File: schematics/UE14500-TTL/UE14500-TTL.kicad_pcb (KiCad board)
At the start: 2 copper layers, 76.8 x 99.1 mm, 43 parts, among them J1 Edge 1, J2 Edge 2, J3 5VDC IN, SW1 Power On, U1 74LS08, U10 74LS74, U11 74LS00, U12 74LS86, U13 74LS00, U14 74LS251, U15 74LS02, U16 74LS74, U2 74LS08, U3 74LS00, U4 74LS374, U5 74LS138, U6 74LS138, U7 74LS74, U8 74LS02, U9 74LS02

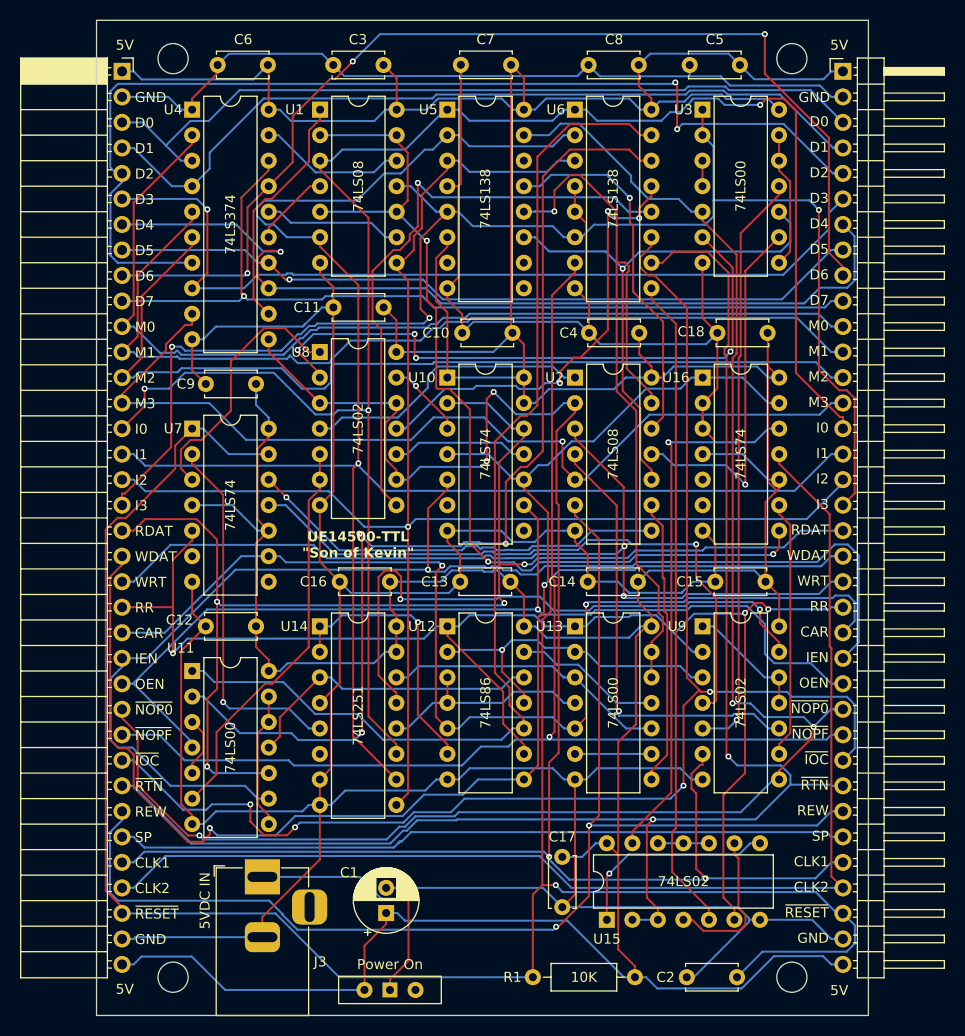
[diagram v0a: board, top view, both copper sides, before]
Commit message: Fix WRITE gating on processor board
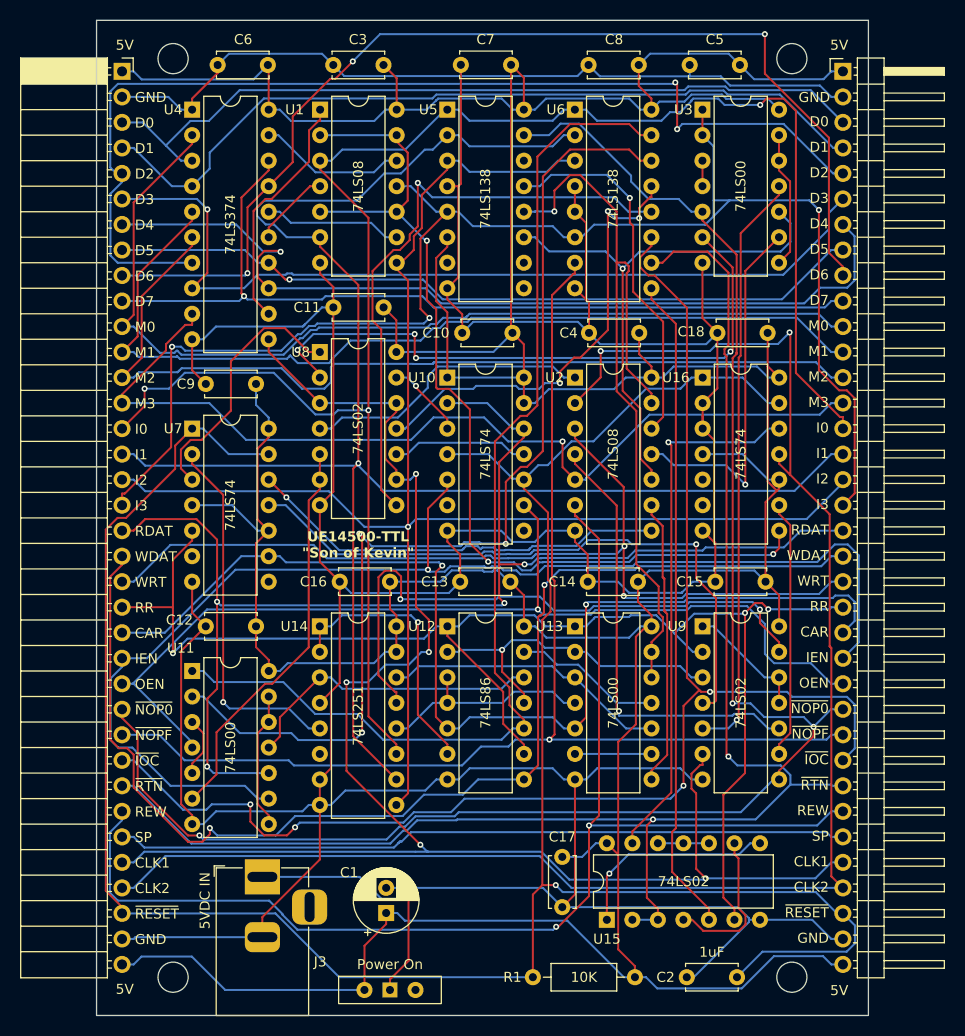
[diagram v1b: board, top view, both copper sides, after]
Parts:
- C2: value 100nF -> 1uF
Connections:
- U2 pad 2: CLK1 -> CLK2
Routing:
- net CLK2: track 120.4 -> 160.4 mm, vias 0 -> 2
- net CLK1: track 185.2 -> 162.4 mm, vias 4 -> 5
- net INST3: track 145.5 -> 147.7 mm

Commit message: Update the CPU schematic with V2 modifications
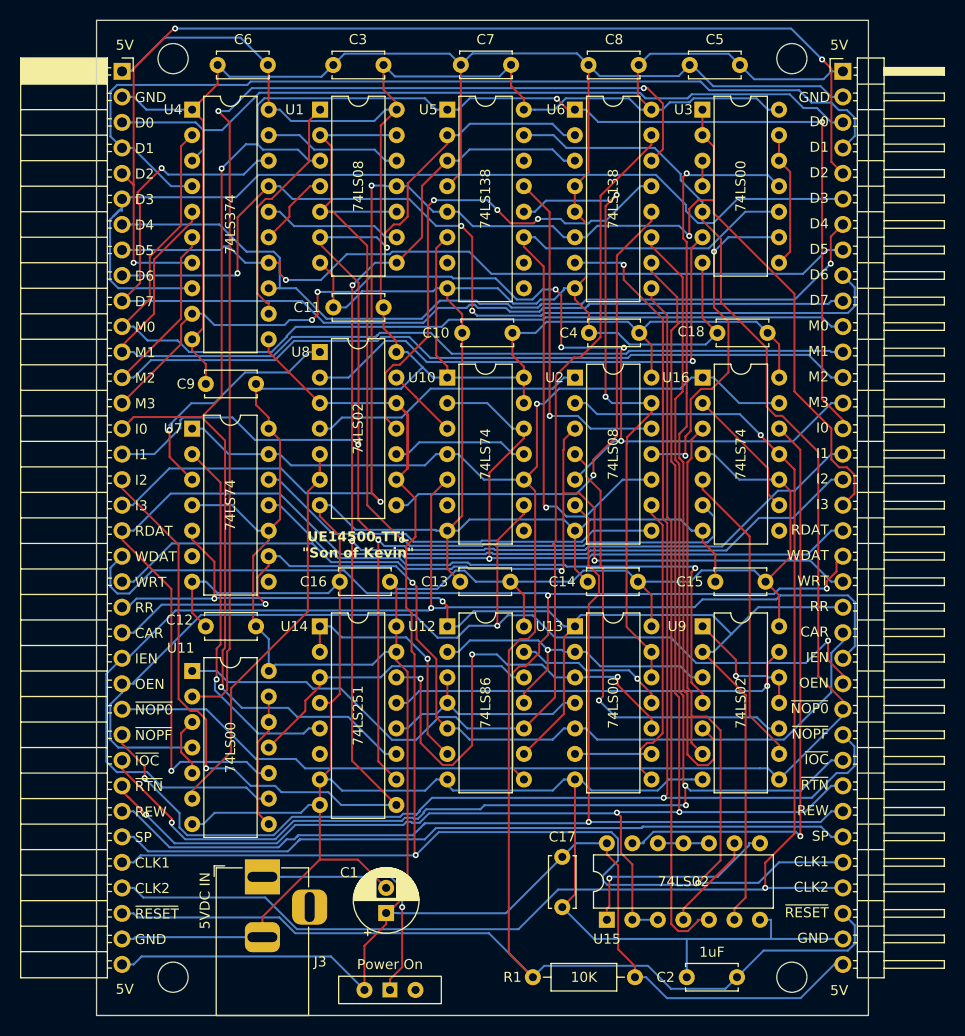
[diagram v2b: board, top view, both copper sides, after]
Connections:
- U16 pad 2: GND -> Net-(U16A-D)
- U16 pad 3: GND -> CLK1
- U16 pad 5: unconnected-(U16A-Q-Pad5) -> SKIP
- U16 pad 6: unconnected-(U16A-~{Q}-Pad6) -> ~{SKIP}
- U16 pad 8: ~{SKIP} -> unconnected-(U16B-~{Q}-Pad8)
- U16 pad 9: SKIP -> Net-(U16A-D)
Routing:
- net CLK1: track 162.4 -> 204.5 mm, vias 5 -> 2
- net ~{RESET}: track 244.4 -> 205.2 mm
- net INST2: track 156.9 -> 190.4 mm, vias 1 -> 3
- net ~{OP_NOPF}: track 123.1 -> 145.6 mm, vias 1 -> 3
- net WR_DATA: track 121.0 -> 101.9 mm
- net OR_RESULT: track 60.5 -> 41.5 mm, vias 2 -> 1
- net GND: track 499.7 -> 481.0 mm
- net NAND_RESULT: track 28.4 -> 46.8 mm, vias 0 -> 3
- net CLK2: track 160.4 -> 142.6 mm
- net REWIND: track 125.5 -> 108.0 mm, vias 2 -> 1
- net ~{LOAD_CAR}: track 58.6 -> 75.4 mm
- net D7: track 87.7 -> 101.3 mm
- net ~{OP_SUB}: track 78.3 -> 64.7 mm, vias 1 -> 2
- net D1: track 80.6 -> 94.2 mm
- net D6: track 107.7 -> 94.3 mm
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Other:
- board text added: "Design by Rhys Weatherley, Version 2, July 2025"
- board text removed: "Design by Rhys Weatherley, Version 1, July 2025"
